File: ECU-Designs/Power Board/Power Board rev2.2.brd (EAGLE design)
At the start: 59.9 x 79.7 mm, 58 parts, among them X1 MINIFIT_5566-2, X2 MINIFIT_5566-6

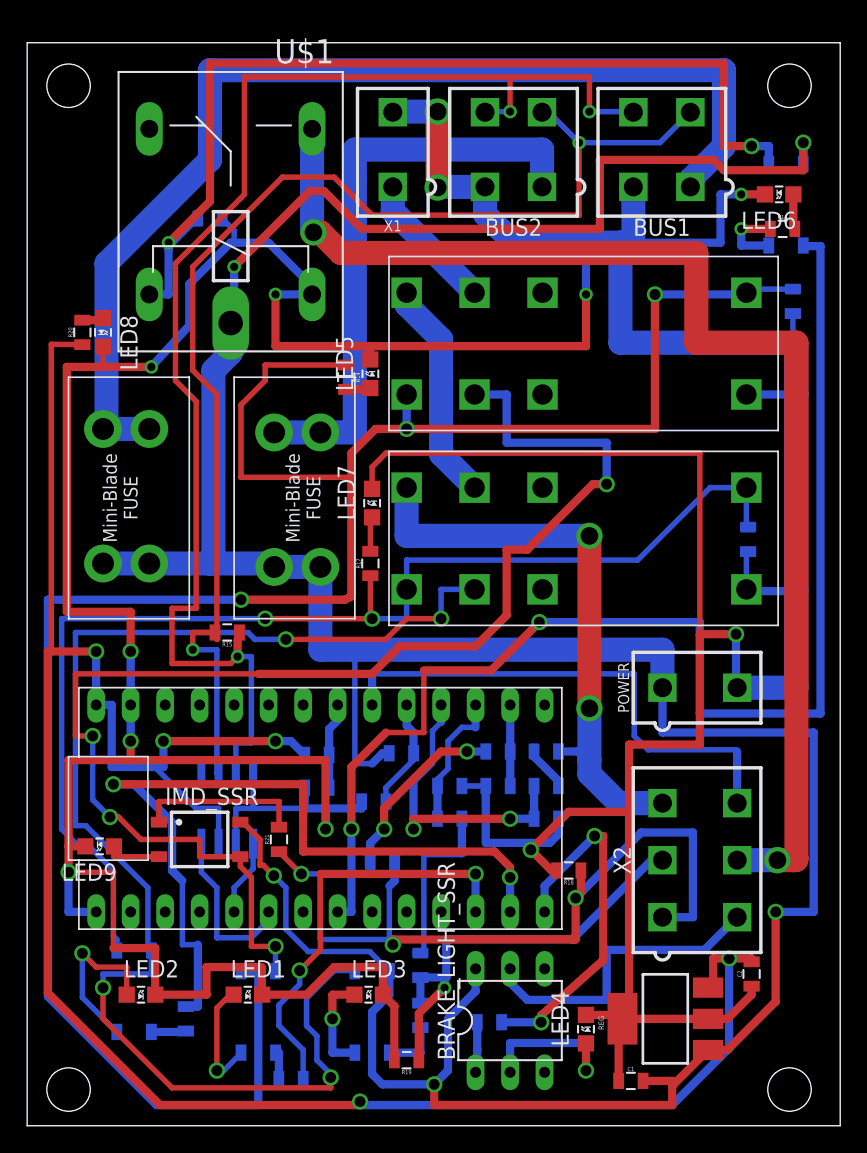
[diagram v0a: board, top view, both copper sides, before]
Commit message: Move files, upload final designs with logos, update jeff bms layout for rules compliance
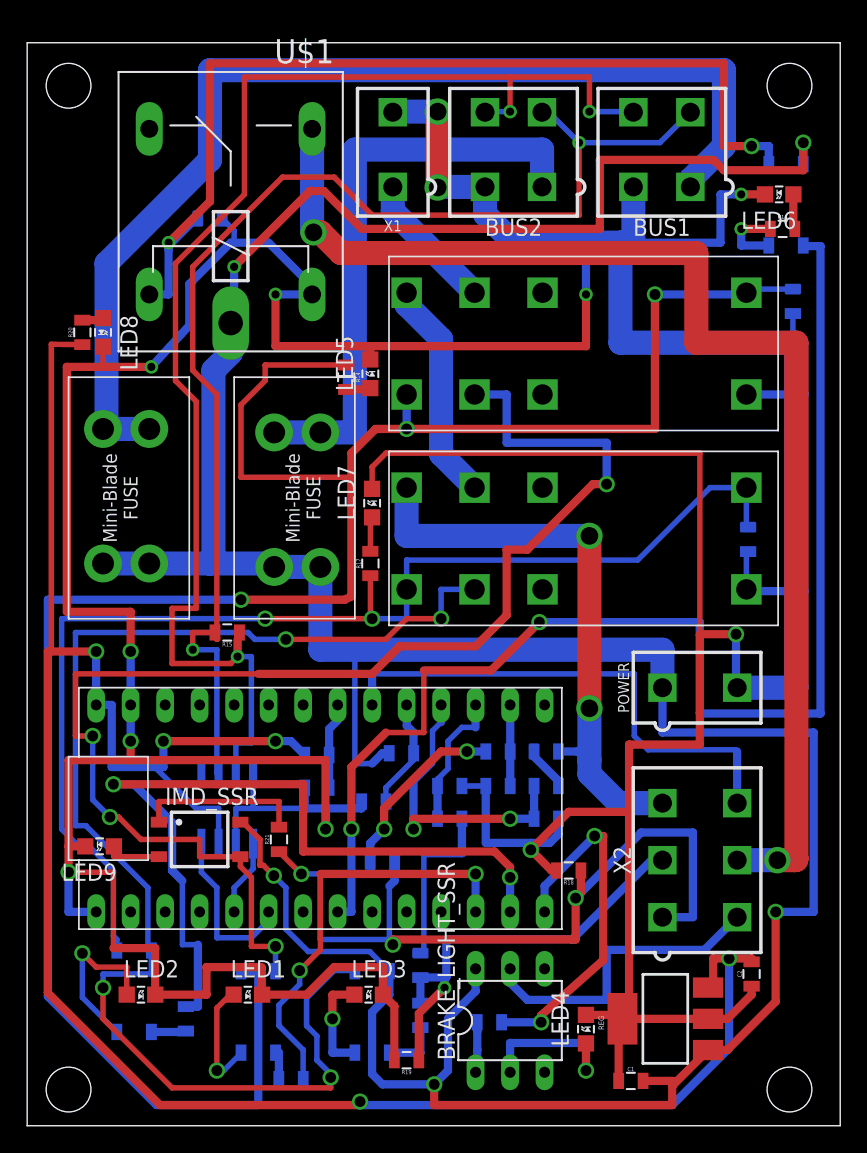
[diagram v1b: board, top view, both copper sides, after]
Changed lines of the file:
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@@
 <setting verticaltext="up"/>
 </settings>
-<grid distance="0.1" unitdist="inch" unit="inch" style="lines" multiple="1" display="yes" altdistance="0.025" altunitdist="inch" altunit="inch"/>
+<grid distance="1" unitdist="mm" unit="mm" style="lines" multiple="1" display="yes" altdistance="0.025" altunitdist="inch" altunit="inch"/>
 <layers>
 <layer number="1" name="Top" color="4" fill="1" visible="yes" active="yes"/>
@@
 <wire x1="59.868" y1="79.746" x2="0" y2="79.746" width="0" layer="20"/>
 <wire x1="0" y1="79.746" x2="0" y2="0" width="0" layer="20"/>
-<hole x="3.048" y="76.581" drill="3.2"/>
-<hole x="56.134" y="76.581" drill="3.2"/>
-<hole x="3.048" y="2.667" drill="3.2"/>
-<hole x="56.134" y="2.667" drill="3.2"/>
+<hole x="3.048" y="76.581" drill="3.3"/>
+<hole x="56.134" y="76.581" drill="3.3"/>
+<hole x="3.048" y="2.667" drill="3.3"/>
+<hole x="56.134" y="2.667" drill="3.3"/>
 <text x="6.096" y="5.08" size="0.762" layer="51">BMS LATCH</text>
 <text x="15.24" y="5.08" size="0.762" layer="51">IMD LATCH</text>
